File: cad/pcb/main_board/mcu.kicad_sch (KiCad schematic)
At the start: 13 parts, among them J2 Conn_ARM_JTAG_SWD_10, U1 STM32F401R_B-C_Tx, Y1 Crystal_GND23

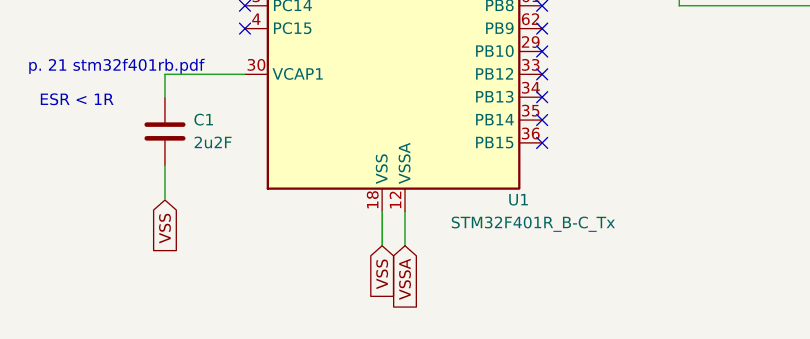
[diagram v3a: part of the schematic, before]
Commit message: DRC mostly checks out now
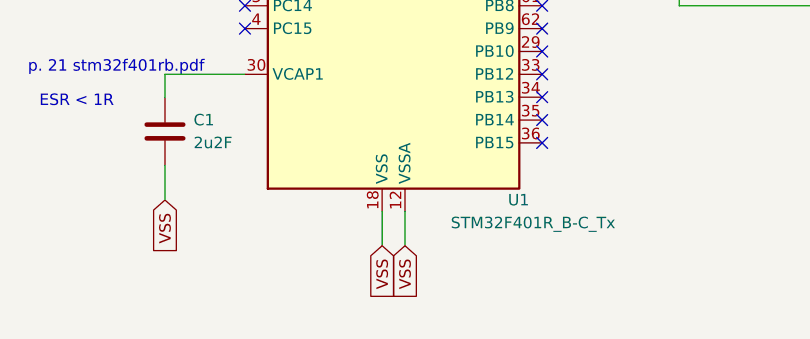
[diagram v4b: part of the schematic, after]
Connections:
- net VSS: now also U1.12 (VSSA)
- net VSSA: no longer U1.12 (VSSA)
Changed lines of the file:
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@@
 		)
 	)
-	(global_label "VSSA"
+	(global_label "VDD"
+		(shape input)
+		(at 260.35 95.25 90)
+		(fields_autoplaced yes)
+		(effects
+			(font
+				(size 1.27 1.27)
+			)
+			(justify left)
+		)
+		(property "Intersheetrefs" "${INTERSHEET_REFS}"
+			(at 260.35 88.6362 90)
+			(effects
+				(font
+					(size 1.27 1.27)
+				)
+				(justify left)
+				(hide yes)
+			)
+		)
+	)
+	(global_label "VDD"
+		(shape input)
+		(at 165.1 52.07 90)
+		(fields_autoplaced yes)
+		(effects
+			(font
+				(size 1.27 1.27)
+			)
+			(justify left)
+		)
+		(property "Intersheetrefs" "${INTERSHEET_REFS}"
+			(at 165.1 45.4562 90)
+			(effects
+				(font
+					(size 1.27 1.27)
+				)
+				(justify left)
+				(hide yes)
+			)
+		)
+	)
+	(global_label "BOOT1"
+		(shape input)
+		(at 266.7 40.64 0)
+		(fields_autoplaced yes)
+		(effects
+			(font
+				(size 1.27 1.27)
+			)
+			(justify left)
+		)
+		(property "Intersheetrefs" "${INTERSHEET_REFS}"
+			(at 275.7933 40.64 0)
+			(effects
+				(font
+					(size 1.27 1.27)
+				)
+				(justify left)
+				(hide yes)
+			)
+		)
+	)
+	(global_label "VSS"
+		(shape input)
+		(at 245.11 138.43 270)
+		(fields_autoplaced yes)
+		(effects
+			(font
+				(size 1.27 1.27)
+			)
+			(justify right)
+		)
+		(property "Intersheetrefs" "${INTERSHEET_REFS}"
+			(at 245.11 144.9228 90)
+			(effects
+				(font
+					(size 1.27 1.27)
+				)
+				(justify right)
+				(hide yes)
+			)
+		)
+	)
+	(global_label "VDD"
+		(shape input)
+		(at 36.83 25.4 0)
+		(fields_autoplaced yes)
+		(effects
+			(font
+				(size 1.27 1.27)
+			)
+			(justify left)
+		)
+		(property "Intersheetrefs" "${INTERSHEET_REFS}"
+			(at 43.4438 25.4 0)
+			(effects
+				(font
+					(size 1.27 1.27)
+				)
+				(justify left)
+				(hide yes)
+			)
+		)
+	)
+	(global_label "VSS"
+		(shape input)
+		(at 114.3 44.45 90)
+		(fields_autoplaced yes)
+		(effects
+			(font
+				(size 1.27 1.27)
+			)
+			(justify left)
+		)
+		(property "Intersheetrefs" "${INTERSHEET_REFS}"
+			(at 114.3 37.9572 90)
+			(effects
+				(font
+					(size 1.27 1.27)
+				)
+				(justify left)
+				(hide yes)
+			)
+		)
+	)
+	(global_label "VSS"
+		(shape input)
+		(at 143.51 144.78 270)
+		(fields_autoplaced yes)
+		(effects
+			(font
+				(size 1.27 1.27)
+			)
+			(justify right)
+		)
+		(property "Intersheetrefs" "${INTERSHEET_REFS}"
+			(at 143.51 151.2728 90)
+			(effects
+				(font
+					(size 1.27 1.27)
+				)
+				(justify right)
+				(hide yes)
+			)
+		)
+	)
+	(global_label "BOOT1"
+		(shape input)
+		(at 191.77 107.95 0)
+		(fields_autoplaced yes)
+		(effects
+			(font
+				(size 1.27 1.27)
+			)
+			(justify left)
+		)
+		(property "Intersheetrefs" "${INTERSHEET_REFS}"
+			(at 200.8633 107.95 0)
+			(effects
+				(font
+					(size 1.27 1.27)
+				)
+				(justify left)
+				(hide yes)
+			)
+		)
+	)
+	(global_label "VSS"
+		(shape input)
+		(at 134.62 44.45 90)
+		(fields_autoplaced yes)
+		(effects
+			(font
+				(size 1.27 1.27)
+			)
+			(justify left)
+		)
+		(property "Intersheetrefs" "${INTERSHEET_REFS}"
+			(at 134.62 37.9572 90)
+			(effects
+				(font
+					(size 1.27 1.27)
+				)
+				(justify left)
+				(hide yes)
+			)
+		)
+	)
+	(global_label "VDD"
+		(shape input)
+		(at 172.72 52.07 90)
+		(fields_autoplaced yes)
+		(effects
+			(font
+				(size 1.27 1.27)
+			)
+			(justify left)
+		)
+		(property "Intersheetrefs" "${INTERSHEET_REFS}"
+			(at 172.72 45.4562 90)
+			(effects
+				(font
+					(size 1.27 1.27)
+				)
+				(justify left)
+				(hide yes)
+			)
+		)
+	)
+	(global_label "VDDA"
+		(shape input)
+		(at 147.32 69.85 180)
+		(fields_autoplaced yes)
+		(effects
+			(font
+				(size 1.27 1.27)
+			)
+			(justify right)
+		)
+		(property "Intersheetrefs" "${INTERSHEET_REFS}"
+			(at 139.6176 69.85 0)
+			(effects
+				(font
+					(size 1.27 1.27)
+				)
+				(justify right)
+				(hide yes)
+			)
+		)
+	)
+	(global_label "VSS"
 		(shape input)
 		(at 170.18 149.86 270)
@@
 		)
 		(property "Intersheetrefs" "${INTERSHEET_REFS}"
-			(at 170.18 157.4414 90)
-			(effects
-				(font
-					(size 1.27 1.27)
-				)
-				(justify right)
-				(hide yes)
-			)
-		)
-	)
-	(global_label "VDD"
-		(shape input)
-		(at 260.35 95.25 90)
-		(fields_autoplaced yes)
-		(effects
-			(font
-				(size 1.27 1.27)
-			)
-			(justify left)
-		)
-		(property "Intersheetrefs" "${INTERSHEET_REFS}"
-			(at 260.35 88.6362 90)
-			(effects
-				(font
-					(size 1.27 1.27)
-				)
-				(justify left)
-				(hide yes)
-			)
-		)
-	)
-	(global_label "VDD"
-		(shape input)
-		(at 165.1 52.07 90)
-		(fields_autoplaced yes)
-		(effects
-			(font
-				(size 1.27 1.27)
-			)
-			(justify left)
-		)
-		(property "Intersheetrefs" "${INTERSHEET_REFS}"
-			(at 165.1 45.4562 90)
-			(effects
-				(font
-					(size 1.27 1.27)
-				)
-				(justify left)
-				(hide yes)
-			)
-		)
-	)
-	(global_label "BOOT1"
-		(shape input)
-		(at 266.7 40.64 0)
-		(fields_autoplaced yes)
-		(effects
-			(font
-				(size 1.27 1.27)
-			)
-			(justify left)
-		)
-		(property "Intersheetrefs" "${INTERSHEET_REFS}"
-			(at 275.7933 40.64 0)
-			(effects
-				(font
-					(size 1.27 1.27)
-				)
-				(justify left)
-				(hide yes)
-			)
-		)
-	)
-	(global_label "VSS"
-		(shape input)
-		(at 245.11 138.43 270)
-		(fields_autoplaced yes)
-		(effects
-			(font
-				(size 1.27 1.27)
-			)
-			(justify right)
-		)
-		(property "Intersheetrefs" "${INTERSHEET_REFS}"
-			(at 245.11 144.9228 90)
-			(effects
-				(font
-					(size 1.27 1.27)
-				)
-				(justify right)
-				(hide yes)
-			)
-		)
-	)
-	(global_label "VDD"
-		(shape input)
-		(at 36.83 25.4 0)
-		(fields_autoplaced yes)
-		(effects
-			(font
-				(size 1.27 1.27)
-			)
-			(justify left)
-		)
-		(property "Intersheetrefs" "${INTERSHEET_REFS}"
-			(at 43.4438 25.4 0)
-			(effects
-				(font
-					(size 1.27 1.27)
-				)
-				(justify left)
-				(hide yes)
-			)
-		)
-	)
-	(global_label "VSS"
-		(shape input)
-		(at 114.3 44.45 90)
-		(fields_autoplaced yes)
-		(effects
-			(font
-				(size 1.27 1.27)
-			)
-			(justify left)
-		)
-		(property "Intersheetrefs" "${INTERSHEET_REFS}"
-			(at 114.3 37.9572 90)
-			(effects
-				(font
-					(size 1.27 1.27)
-				)
-				(justify left)
-				(hide yes)
-			)
-		)
-	)
-	(global_label "VSS"
-		(shape input)
-		(at 143.51 144.78 270)
-		(fields_autoplaced yes)
-		(effects
-			(font
-				(size 1.27 1.27)
-			)
-			(justify right)
-		)
-		(property "Intersheetrefs" "${INTERSHEET_REFS}"
-			(at 143.51 151.2728 90)
-			(effects
-				(font
-					(size 1.27 1.27)
-				)
-				(justify right)
-				(hide yes)
-			)
-		)
-	)
-	(global_label "BOOT1"
-		(shape input)
-		(at 191.77 107.95 0)
-		(fields_autoplaced yes)
-		(effects
-			(font
-				(size 1.27 1.27)
-			)
-			(justify left)
-		)
-		(property "Intersheetrefs" "${INTERSHEET_REFS}"
-			(at 200.8633 107.95 0)
-			(effects
-				(font
-					(size 1.27 1.27)
-				)
-				(justify left)
-				(hide yes)
-			)
-		)
-	)
-	(global_label "VSS"
-		(shape input)
-		(at 134.62 44.45 90)
-		(fields_autoplaced yes)
-		(effects
-			(font
-				(size 1.27 1.27)
-			)
-			(justify left)
-		)
-		(property "Intersheetrefs" "${INTERSHEET_REFS}"
-			(at 134.62 37.9572 90)
-			(effects
-				(font
-					(size 1.27 1.27)
-				)
-				(justify left)
-				(hide yes)
-			)
-		)
-	)
-	(global_label "VDD"
-		(shape input)
-		(at 172.72 52.07 90)
-		(fields_autoplaced yes)
-		(effects
-			(font
-				(size 1.27 1.27)
-			)
-			(justify left)
-		)
-		(property "Intersheetrefs" "${INTERSHEET_REFS}"
-			(at 172.72 45.4562 90)
-			(effects
-				(font
-					(size 1.27 1.27)
-				)
-				(justify left)
-				(hide yes)
-			)
-		)
-	)
-	(global_label "VDDA"
-		(shape input)
-		(at 147.32 69.85 180)
-		(fields_autoplaced yes)
-		(effects
-			(font
-				(size 1.27 1.27)
-			)
-			(justify right)
-		)
-		(property "Intersheetrefs" "${INTERSHEET_REFS}"
-			(at 139.6176 69.85 0)
-			(effects
-				(font
+			(at 170.18 156.3528 90)
+			(effects
+				(font

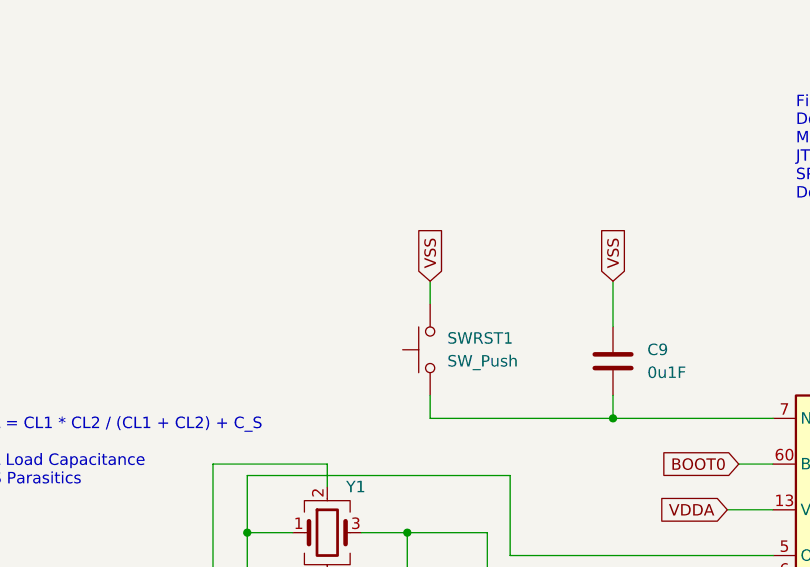
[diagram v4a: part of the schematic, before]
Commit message: Replace Push button with switch
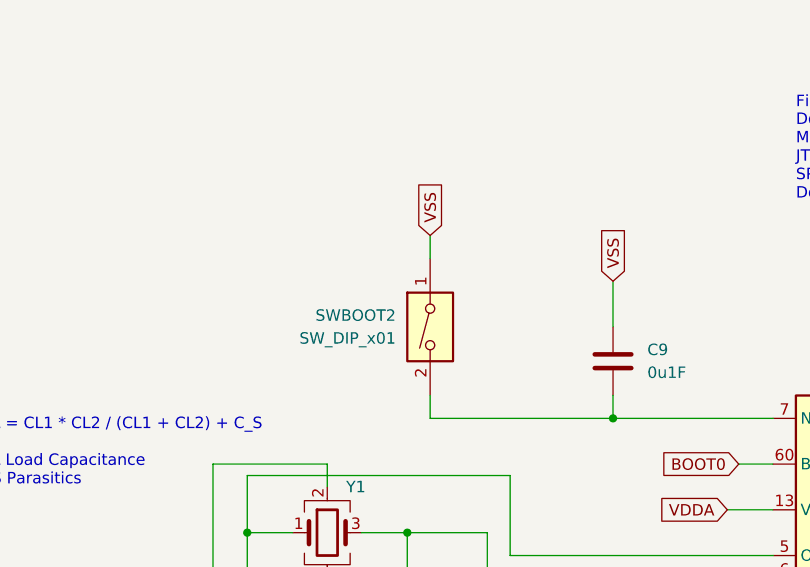
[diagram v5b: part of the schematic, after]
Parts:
- removed SWRST1: SW_Push, Button_Switch_THT:SW_PUSH_6mm, symbol Switch:SW_Push
- added SWBOOT2: SW_DIP_x01, Button_Switch_SMD:SW_DIP_SPSTx01_Slide_6.7x4.1mm_W6.73mm_P2.54mm_LowProfile_JPin, symbol Switch:SW_DIP_x01
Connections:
- net VSS: now also SWBOOT2.1
- net at C9.2, U1.7 (NRST): now also SWBOOT2.2
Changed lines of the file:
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@@
 	(wire
 		(pts
-			(xy 114.3 44.45) (xy 114.3 46.99)
+			(xy 114.3 39.37) (xy 114.3 41.91)
 		)
 		(stroke
@@
 	(global_label "VSS"
 		(shape input)
-		(at 114.3 44.45 90)
-		(fields_autoplaced yes)
-		(effects
-			(font
-				(size 1.27 1.27)
-			)
-			(justify left)
-		)
-		(property "Intersheetrefs" "${INTERSHEET_REFS}"
-			(at 114.3 37.9572 90)
+		(at 114.3 39.37 90)
+		(fields_autoplaced yes)
+		(effects
+			(font
+				(size 1.27 1.27)
+			)
+			(justify left)
+		)
+		(property "Intersheetrefs" "${INTERSHEET_REFS}"
+			(at 114.3 32.8772 90)
 			(effects
 				(font
@@
 			)
 			(justify left)
+		)
+	)
+	(symbol
+		(lib_id "Switch:SW_DIP_x01")
+		(at 114.3 49.53 90)
+		(mirror x)
+		(unit 1)
+		(exclude_from_sim no)
+		(in_bom yes)
+		(on_board yes)
+		(dnp no)
+		(property "Reference" "SWBOOT2"
+			(at 110.49 48.2599 90)
+			(effects
+				(font
+					(size 1.27 1.27)
+				)
+				(justify left)
+			)
+		)
+		(property "Value" "SW_DIP_x01"
+			(at 110.49 50.7999 90)
+			(effects
+				(font
+					(size 1.27 1.27)
+				)
+				(justify left)
+			)
+		)
+		(property "Footprint" "Button_Switch_SMD:SW_DIP_SPSTx01_Slide_6.7x4.1mm_W6.73mm_P2.54mm_LowProfile_JPin"
+			(at 114.3 49.53 0)
+			(effects
+				(font
+					(size 1.27 1.27)
+				)
+				(hide yes)
+			)
+		)
+		(property "Datasheet" "~"
+			(at 114.3 49.53 0)
+			(effects
+				(font
+					(size 1.27 1.27)
+				)
+				(hide yes)
+			)
+		)
+		(property "Description" "1x DIP Switch, Single Pole Single Throw (SPST) switch, small symbol"
+			(at 114.3 49.53 0)
+			(effects
+				(font
+					(size 1.27 1.27)
+				)
+				(hide yes)
+			)
+		)
+		(pin "1"
+		)
+		(pin "2"
+		)
+		(instances
+			(project "main_board"
+				(path "/6c1b8035-64fa-4797-a506-5c9583cb241c/89e1b759-e3da-4961-90e8-6f92bf79e795"
+					(reference "SWBOOT2")
+					(unit 1)
+				)
+			)
 		)
 	)
@@
 					(unit 1)
 				)
-			)
-		)
-	)
-	(symbol
-		(lib_id "Switch:SW_Push")
-		(at 114.3 52.07 90)
-		(unit 1)
-		(exclude_from_sim no)
-		(in_bom yes)
-		(on_board yes)
-		(dnp no)
-		(fields_autoplaced yes)
-		(property "Reference" "SWRST1"
-			(at 116.205 50.8 90)
-			(effects
-				(font
-					(size 1.27 1.27)
-				)
-				(justify right)
-			)
-		)
-		(property "Value" "SW_Push"
-			(at 116.205 53.34 90)
-			(effects
-				(font
-					(size 1.27 1.27)
-				)
-				(justify right)
-			)
-		)
-		(property "Footprint" "Button_Switch_THT:SW_PUSH_6mm"
-			(at 109.22 52.07 0)
-			(effects
-				(font
-					(size 1.27 1.27)
-				)
-				(hide yes)
-			)
-		)
-		(property "Datasheet" "~"
-			(at 109.22 52.07 0)
-			(effects
-				(font
-					(size 1.27 1.27)
-				)
-				(hide yes)
-			)
-		)
-		(property "Description" "Push button switch, generic, two pins"
-			(at 114.3 52.07 0)
-			(effects
-				(font
-					(size 1.27 1.27)
-				)
-				(hide yes)
-			)
-		)
-		(pin "1"
-		)
-		(pin "2"
-		)
-		(instances
-			(project "main_board"
-				(path "/6c1b8035-64fa-4797-a506-5c9583cb241c/89e1b759-e3da-4961-90e8-6f92bf79e795"
-					(reference "SWRST1")
-					(unit 1)
-				)
